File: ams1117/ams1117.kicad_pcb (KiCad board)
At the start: 2 copper layers, 26.7 x 11.4 mm, 7 parts, among them J1 PWR_IN, J2 PWR_OUT, U1 AMS1117

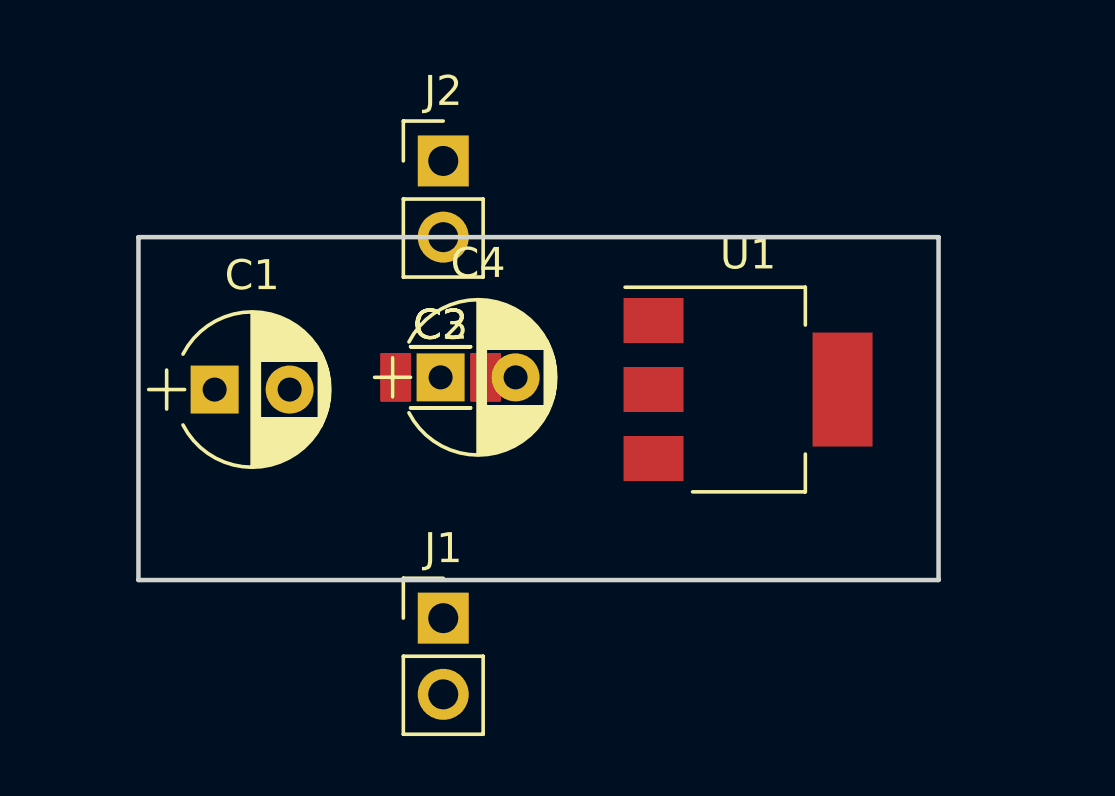
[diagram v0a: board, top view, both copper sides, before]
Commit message: 完成AMS1117降压模块PCB绘制
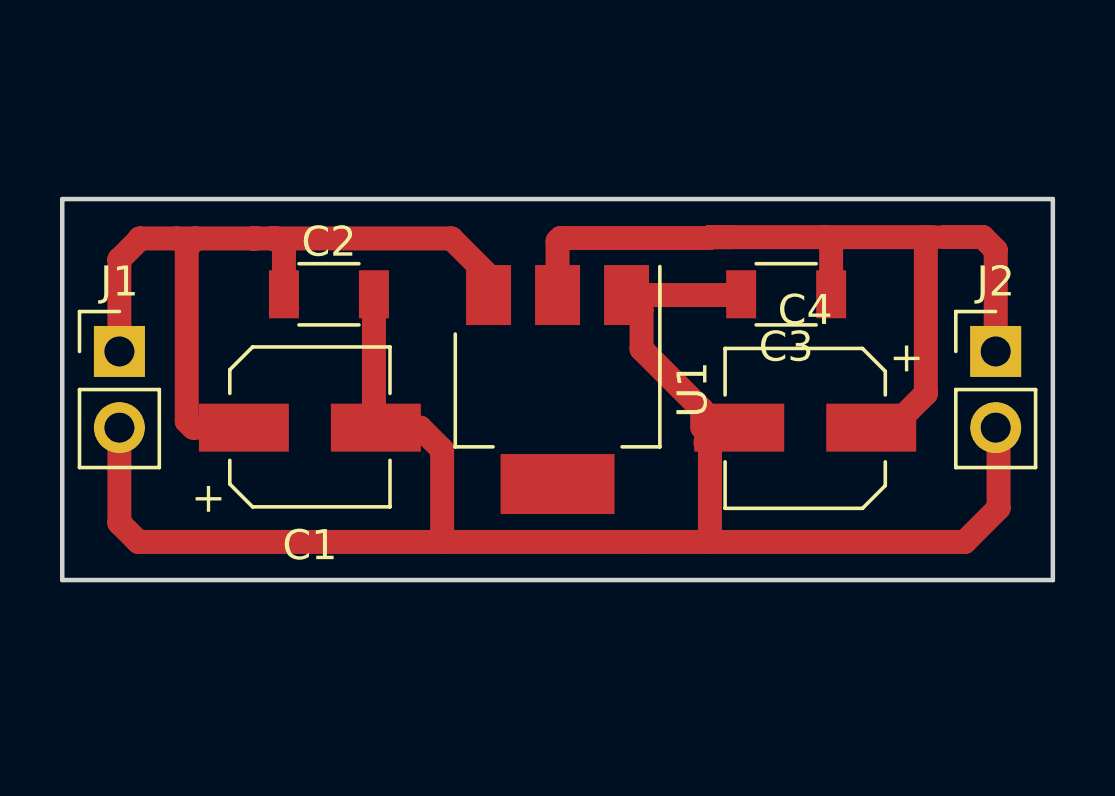
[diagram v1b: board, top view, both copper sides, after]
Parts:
- C1, C4: footprint Capacitors_THT:CP_Radial_D5.0mm_P2.50mm -> Capacitors_SMD:CP_Elec_5x5.3
- moved J2 19.5 mm to (167.0, 104.1)
- moved J1 14.0 mm to (137.8, 104.1)
- moved C4 12.3 mm to (160.7, 106.7), turned to 180 degrees
- moved C3 11.8 mm to (160.0, 102.2), turned to 180 degrees
- moved U1 6.35 mm to (152.4, 105.4), turned to 270 degrees
- moved C2 4.64 mm to (144.8, 102.2)
- moved C1 3.42 mm to (144.1, 106.7)
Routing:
- net GND: track 0.00 -> 58.6 mm
- net +3V3: track 0.00 -> 30.6 mm
- net +5V: track 0.00 -> 28.0 mm
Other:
- board size 26.7 x 11.4 mm -> 33 x 12.7 mm
- rule trace_min: 0.2 -> 0.5
- rule via_min_drill: 0.3 -> 0.5
- rule via_min_size: 0.4 -> 0.8
